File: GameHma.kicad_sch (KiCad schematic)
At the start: 15 parts, among them J1 Screw_Terminal_01x02, J2 Motor_Terminal_01x04, J3 Motor_Terminal_01x04, J4 Motor_Terminal_01x04, J5 Motor_Terminal_01x04, U1 ESP32-DEVKIT-V1, U2 A4988_STEPPER_MOTOR_DRIVER_CA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, U3 A4988_STEPPER_MOTOR_DRIVER_CA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, U4 A4988_STEPPER_MOTOR_DRIVER_CA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, U5 A4988_STEPPER_MOTOR_DRIVER_CA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, U6 SRT_MP1584EN

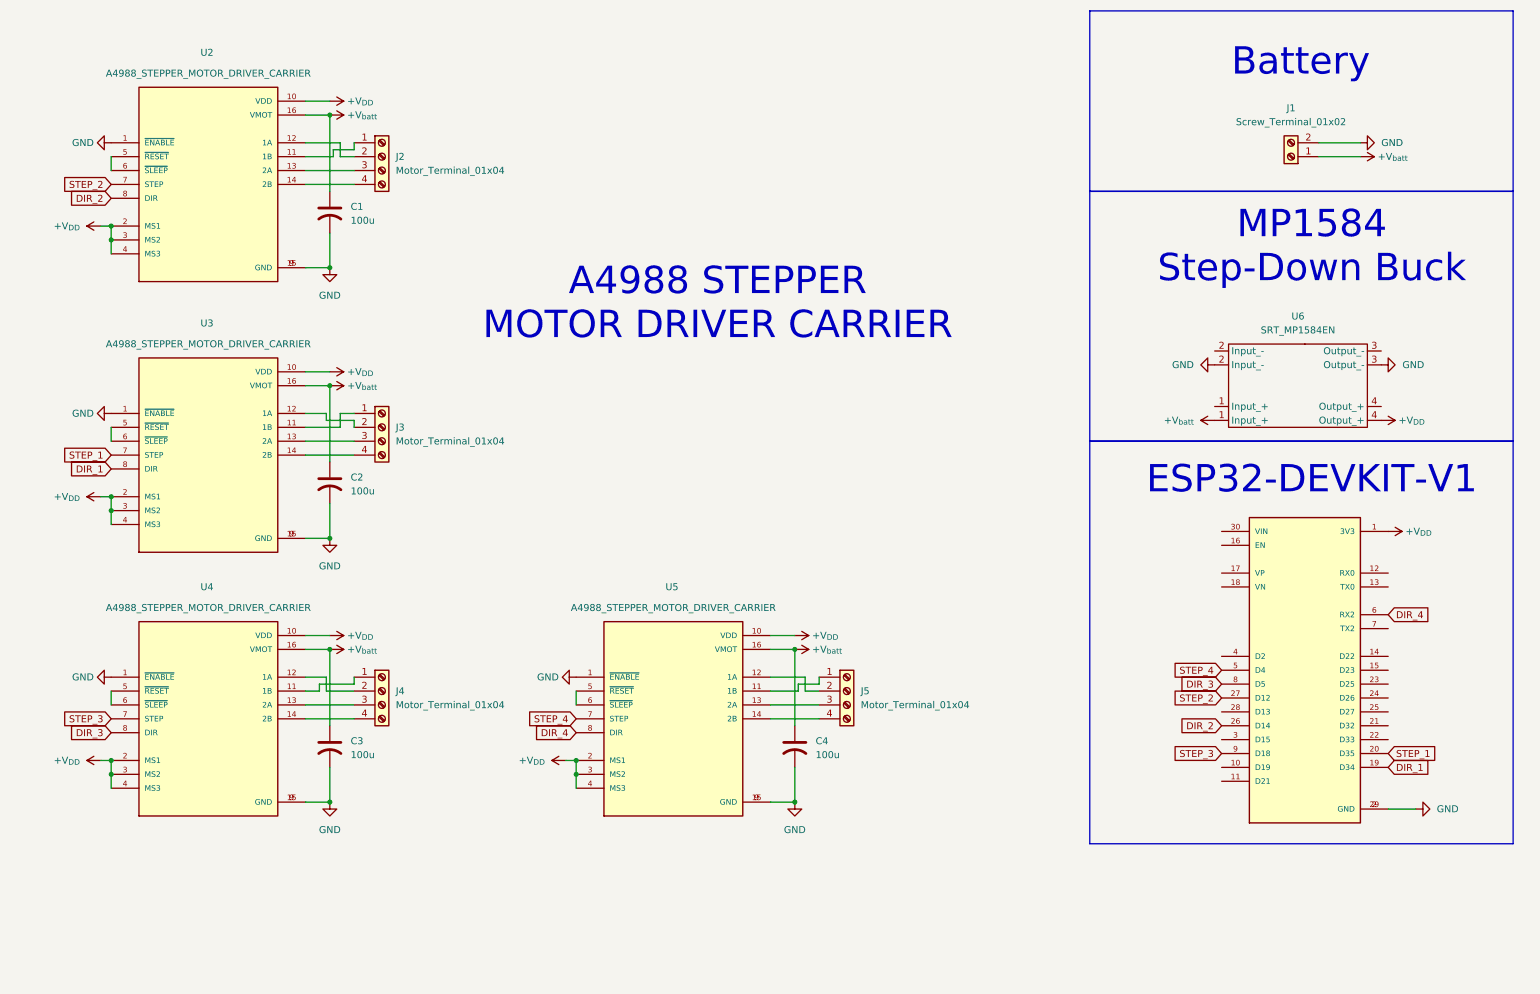
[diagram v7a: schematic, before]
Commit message: add connector for gun
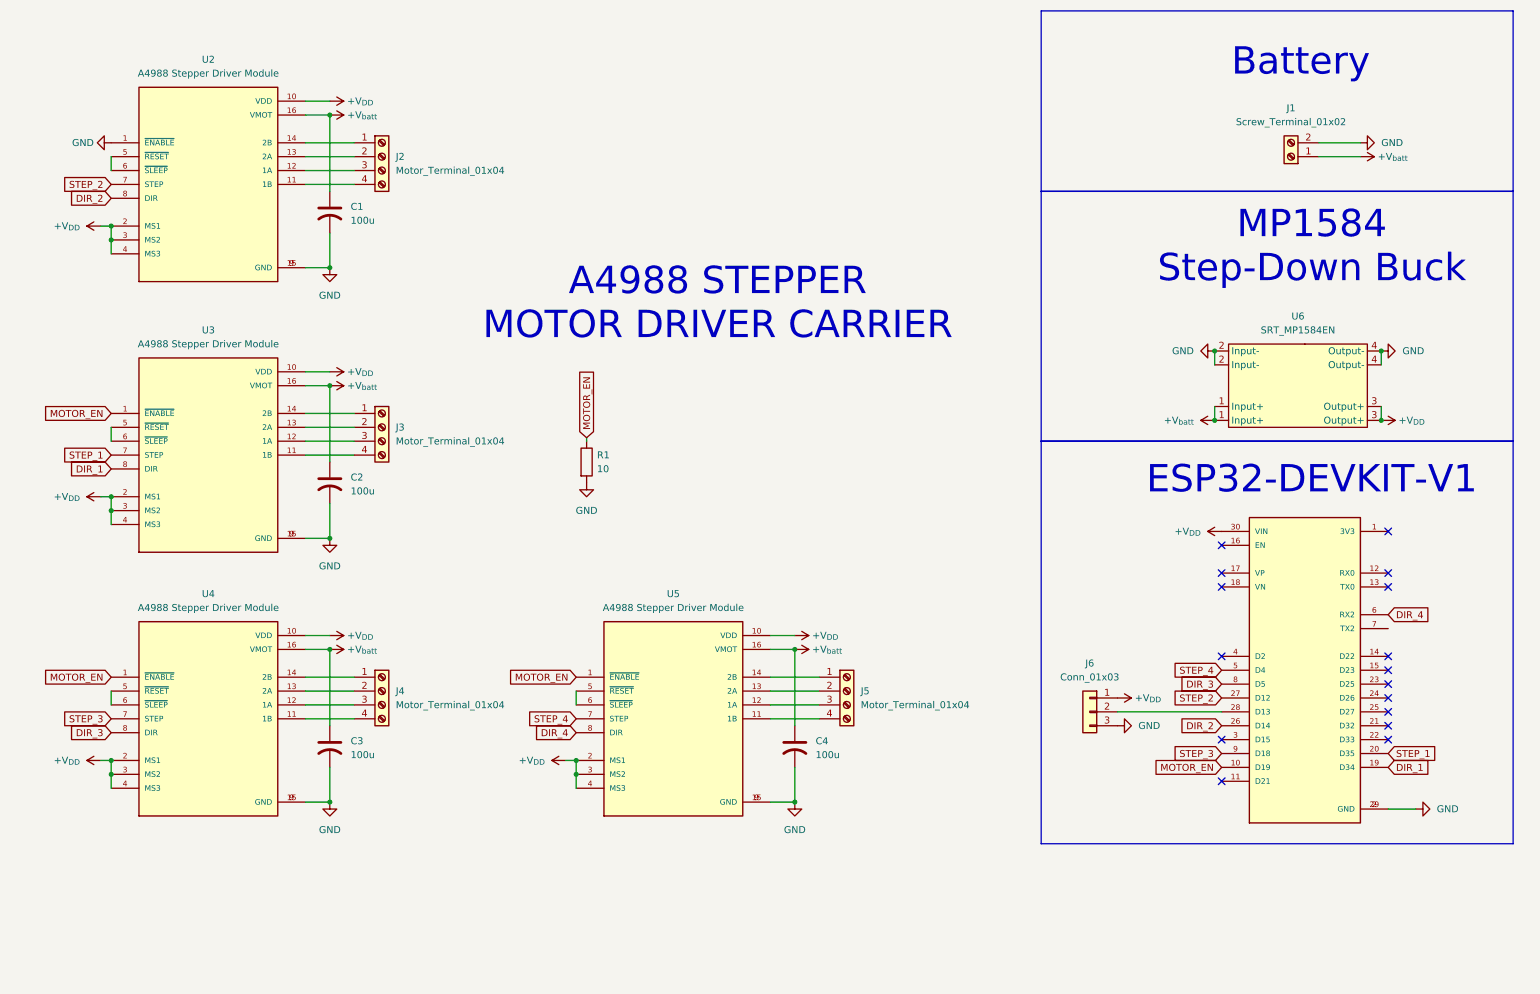
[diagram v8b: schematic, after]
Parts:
- removed U2, U3, U4, U5: A4988_STEPPER_MOTOR_DRIVER_CARRIER, A4988_STEPPER_MOTOR_DRIVER_CARRIER:MODULE_A4988_STEPPER_MOTOR_DRIVER_CARRIER, symbol A4988_STEPPER_MOTOR_DRIVER_CARRIER:A4988_STEPPER_MOTOR_DRIVER_CARRIER
- removed U6: SRT_MP1584EN, SRT:SRT_MPT1584EN_Module, symbol SRT_MP1584EN:SRT_MP1584EN
- added J6: Conn_01x03, Connector_JST:JST_XA_B03B-XASK-1-A_1x03_P2.50mm_Vertical, symbol Connector_Generic:Conn_01x03
- added R1: 10, Resistor_THT:R_Axial_DIN0309_L9.0mm_D3.2mm_P2.54mm_Vertical, symbol Device:R
- added U2, U3, U4, U5: A4988 Stepper Driver Module, Custom Footprint:A4988 Stepper Driver, symbol Custom:A4988 Stepper Driver Module
- added U6: SRT_MP1584EN, Custom Footprint:MPT1584EN_Module, symbol Custom:SRT_MP1584EN
- J2, J3, J4, J5: footprint Connector_JST:JST_EH_B4B-EH-A_1x04_P2.50mm_Vertical -> Connector_JST:JST_XA_B04B-XASK-1-A_1x04_P2.50mm_Vertical
- U1: footprint ESP32-DEVKIT-V1:MODULE_ESP32_DEVKIT_V1 -> Custom Footprint:ESP32 Dev Board
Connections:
- net +V_{DD}: now also U1.30 (VIN), J6.1 (Pin_1), U2.10 (VDD), U2.2 (MS1), U2.3 (MS2), U2.4 (MS3), U3.10 (VDD), U3.2 (MS1), U3.3 (MS2), U3.4 (MS3), U4.10 (VDD), U4.2 (MS1), U4.3 (MS2), U4.4 (MS3), U5.10 (VDD), U5.2 (MS1), U5.3 (MS2), U5.4 (MS3), U6.3 (Output+); no longer U1.1 (3V3)
- net +V_{batt}: now also U2.16 (VMOT), U3.16 (VMOT), U4.16 (VMOT), U5.16 (VMOT), U6.1 (Input+)
- net DIR_1: now also U3.8 (DIR)
- net DIR_2: now also U2.8 (DIR)
- net DIR_3: now also U4.8 (DIR)
- net DIR_4: now also U5.8 (DIR)
- net GND: now also J6.3 (Pin_3), R1.2, U2.1 (~{ENABLE}), U2.15 (GND), U2.9 (GND), U3.15 (GND), U3.9 (GND), U4.15 (GND), U4.9 (GND), U5.15 (GND), U5.9 (GND), U6.2 (Input-), U6.4 (Output-)
- net STEP_1: now also U3.7 (STEP)
- net STEP_2: now also U2.7 (STEP)
- net STEP_3: now also U4.7 (STEP)
- net STEP_4: now also U5.7 (STEP)
- net at J4.1 (Pin_1): now also U4.14 (2B)
- net at J4.2 (Pin_2): now also U4.13 (2A)
- net at J4.3 (Pin_3): now also U4.12 (1A)
- net at J4.4 (Pin_4): now also U4.11 (1B)
- net at J3.1 (Pin_1): now also U3.14 (2B)
- net at J3.2 (Pin_2): now also U3.13 (2A)
- net at J3.3 (Pin_3): now also U3.12 (1A)
- net at J3.4 (Pin_4): now also U3.11 (1B)
- net at J2.1 (Pin_1): now also U2.14 (2B)
- net at J2.2 (Pin_2): now also U2.13 (2A)
- net at J2.3 (Pin_3): now also U2.12 (1A)
- net at J2.4 (Pin_4): now also U2.11 (1B)
- net MOTOR_EN: now reaches U1.10 (D19)
- net MOTOR_EN: now also R1.1, U3.1 (~{ENABLE}), U4.1 (~{ENABLE}), U5.1 (~{ENABLE})
- net at U1.28 (D13): now also J6.2 (Pin_2)
- net at J5.1 (Pin_1): now also U5.14 (2B)
- net at J5.2 (Pin_2): now also U5.13 (2A)
- net at J5.3 (Pin_3): now also U5.12 (1A)
- net at J5.4 (Pin_4): now also U5.11 (1B)
- new net: U4.5 (~{RESET}), U4.6 (~{SLEEP})
- new net: U5.5 (~{RESET}), U5.6 (~{SLEEP})
- new net: U2.5 (~{RESET}), U2.6 (~{SLEEP})
- new net: U3.5 (~{RESET}), U3.6 (~{SLEEP})
- no-connect marks 0 -> 16
